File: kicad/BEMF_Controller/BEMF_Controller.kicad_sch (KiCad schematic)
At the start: 110 parts, among them J1 HEADER4VALULOK, J2 HEADER6, J3 FUSE, J4 Coil_A, J5 Coil_B, J6 Coil_C, J7 Vin, Q1 IGBT-TO-247, Q2 IGBT-TO-247, Q3 IGBT-TO-247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

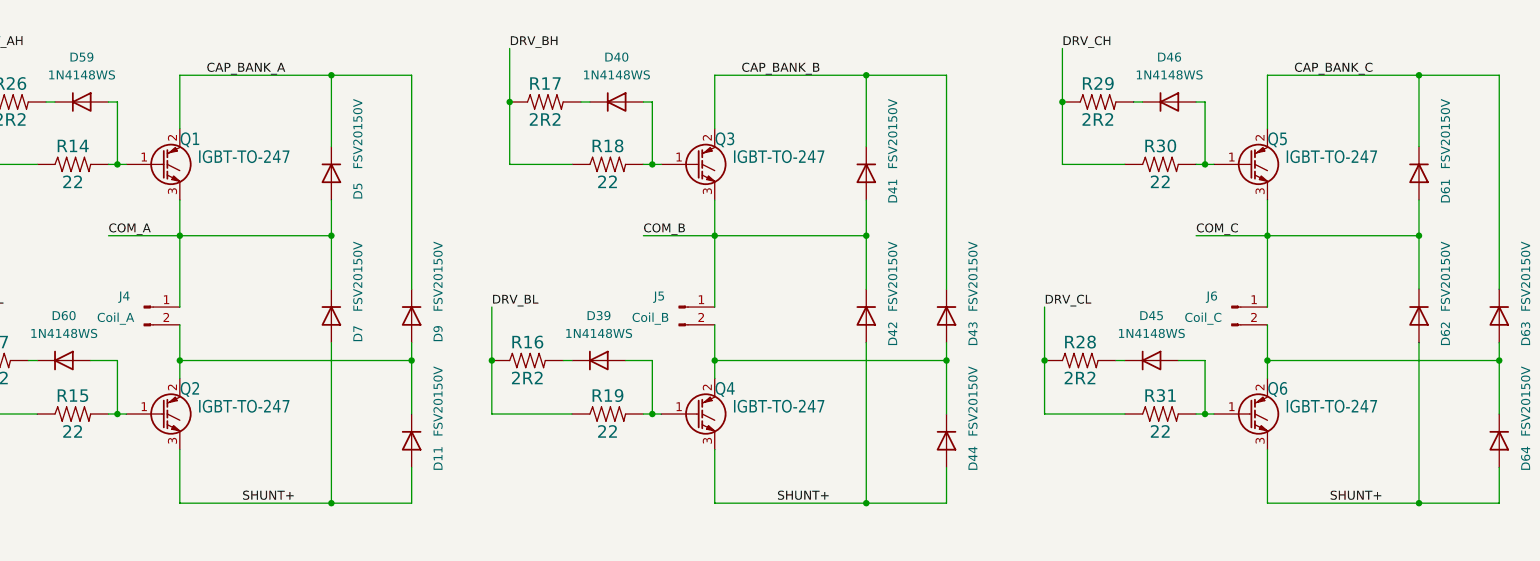
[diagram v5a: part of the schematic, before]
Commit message: Change to mosfets.
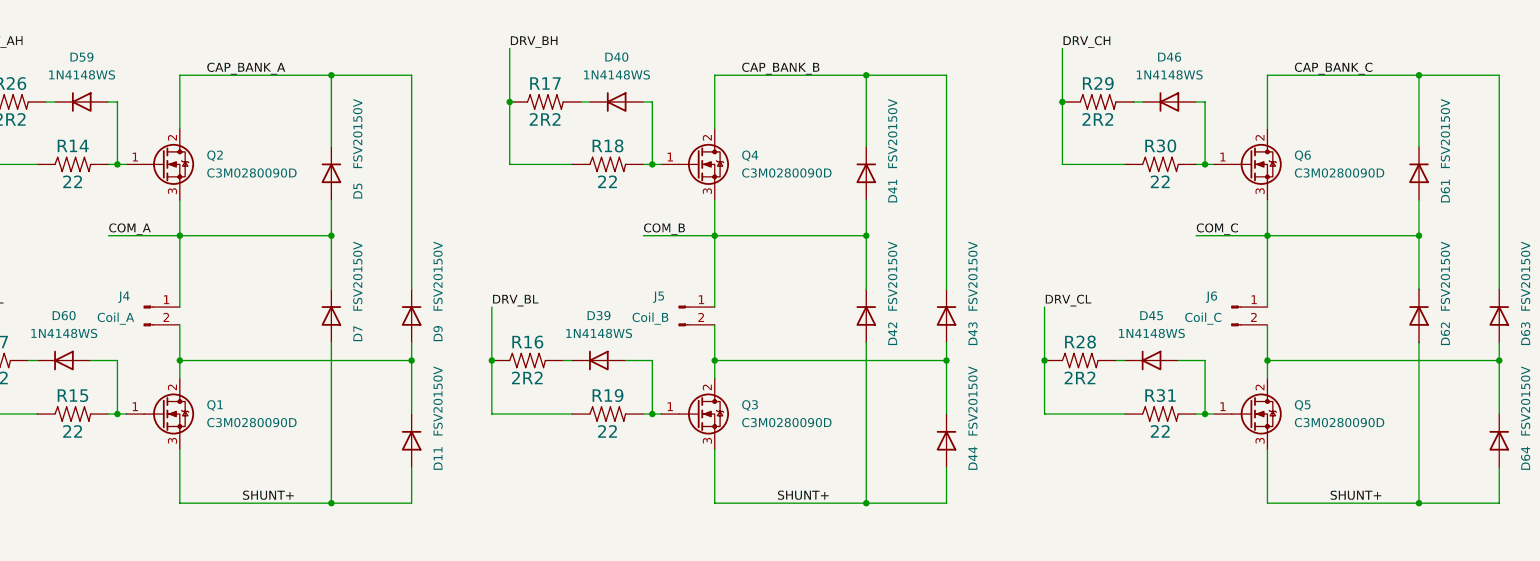
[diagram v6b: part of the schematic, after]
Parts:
- removed Q1, Q2, Q3, Q4, Q5, Q6: IGBT-TO-247, Package_TO_SOT_THT:TO-247-3_Vertical, symbol Transistor_IGBT:IRG4PF50W
- added Q1, Q2, Q3, Q4, Q5, Q6: C3M0280090D, Package_TO_SOT_THT:TO-247-3_Horizontal_TabDown, symbol Transistor_FET:C3M0280090D
- JP7: footprint Connector_PinHeader_2.54mm:PinHeader_1x02_P2.54mm_Vertical -> Jumper:SolderJumper-2_P1.3mm_Open_RoundedPad1.0x1.5mm
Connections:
- net CAP_BANK_A: now also Q2.2 (D)
- net CAP_BANK_B: now also Q4.2 (D)
- net CAP_BANK_C: now also Q6.2 (D)
- net COM_A: now also Q2.3 (S)
- net COM_B: now also Q4.3 (S)
- net COM_C: now also Q6.3 (S)
- net SHUNT+: now also Q1.3 (S), Q3.3 (S), Q5.3 (S)
- net at D40.2 (A), R18.2: now also Q4.1 (G)
- net at D43.2 (A), D44.1 (K), J5.2 (Pin_2): now also Q3.2 (D)
- net at D63.2 (A), D64.1 (K), J6.2 (Pin_2): now also Q5.2 (D)
- net at D11.1 (K), D9.2 (A), J4.2 (Pin_2): now also Q1.2 (D)
- net at D39.2 (A), R19.2: now also Q3.1 (G)
- net at D60.2 (A), R15.2: now also Q1.1 (G)
- net at D46.2 (A), R30.2: now also Q6.1 (G)
- net at D59.2 (A), R14.2: now also Q2.1 (G)
- net at D45.2 (A), R31.2: now also Q5.1 (G)

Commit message: Updated Shottky footprint
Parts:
- removed D39, D40, D45, D46, D59, D60: 1N4148WS, Diode_SMD:D_SOD-323F, symbol Device:D
- removed D41, D42, D43, D44, D61, D62, D63, D64: FSV20150V, Package_TO_SOT_SMD:TO-277A, symbol Device:D
- removed R14, R18, R19, R30, R31: 22, main:1206, symbol main-eagle-import:RESISTOR1206
- removed R16, R17, R26, R27, R28, R29: 2R2, main:1206, symbol main-eagle-import:RESISTOR1206
- added D39, D40, D41, D42, D43, D44, D45, D46: FSV20150V, Package_TO_SOT_SMD:TO-277A, symbol Component_Library:FSV20150V
- added R14, R16, R17, R18, R19: 10, Resistor_THT:R_Axial_DIN0411_L9.9mm_D3.6mm_P15.24mm_Horizontal, symbol Component_Library:ROX1SJ10R
- C1, C11, C12, C14, C15, C16, C17, C18, C19, C2, C20, C3: footprint main:1206 -> Capacitor_SMD:C_1812_4532Metric; symbol main-eagle-import:1.0UF-1206-50V-10% -> Component_Library:CHV1812N250105MXT
- C9: footprint main:1206 -> Capacitor_SMD:C_0805_2012Metric; symbol main-eagle-import:1.0UF-1206-50V-10% -> Component_Library:CHV1812N250105MXT
- D11, D5, D7, D9: symbol Device:D -> Component_Library:FSV20150V
- R15: value 22 -> 10; footprint main:1206 -> Resistor_THT:R_Axial_DIN0411_L9.9mm_D3.6mm_P15.24mm_Horizontal; symbol main-eagle-import:RESISTOR1206 -> Component_Library:ROX1SJ10R
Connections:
- net CAP_BANK_A: now also D5.2 (A), D9.2 (A)
- net CAP_BANK_B: now also Q3.2 (D), D39.1 (A), D39.2 (A), D41.1 (A), D41.2 (A); no longer Q4.2 (D)
- net CAP_BANK_C: now also Q5.2 (D), D43.1 (A), D43.2 (A), D45.1 (A), D45.2 (A); no longer Q6.2 (D)
- net COM_A: now also D5.3 (K), D7.2 (A); no longer D5.2 (A)
- net COM_B: now also Q3.3 (S), D39.3 (K), D40.1 (A), D40.2 (A); no longer Q4.3 (S)
- net COM_C: now also Q5.3 (S), D43.3 (K), D44.1 (A), D44.2 (A); no longer Q6.3 (S)
- net DRV_AH: now also R14.2
- net DRV_AL: now also R15.2; no longer R15.1
- net DRV_BH: now also R16.2
- net DRV_BL: now also R17.2
- net DRV_CH: now also R18.2
- net DRV_CL: now also R19.2
- net SHUNT+: now also D11.3 (K), D7.3 (K), Q4.3 (S), Q6.3 (S), D40.3 (K), D42.3 (K), D44.3 (K), D46.3 (K); no longer D11.2 (A), D7.2 (A), Q3.3 (S), Q5.3 (S)
- net at J5.2 (Pin_2): now also Q4.2 (D), D41.3 (K), D42.1 (A), D42.2 (A); no longer Q3.2 (D)
- net at J6.2 (Pin_2): now also Q6.2 (D), D45.3 (K), D46.1 (A), D46.2 (A); no longer Q5.2 (D)
- net at Q1.1 (G): now also R15.1; no longer R15.2
- net at D11.1 (A), J4.2 (Pin_2), Q1.2 (D): now also D11.2 (A), D9.3 (K); no longer D9.2 (A)
- net at Q3.1 (G): now also R16.1
- net at Q4.1 (G): now also R17.1
- net at Q2.1 (G): now also R14.1
- net at Q5.1 (G): now also R18.1
- net at Q6.1 (G): now also R19.1

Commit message: Added component library
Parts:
- D49, D50, D53, D54, D57, D58: footprint Diode_SMD:D_SOD-323F -> Diode_SMD:D_SOD-323; symbol Device:D -> Diode:1N4148WS
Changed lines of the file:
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@@
 	)
 	(symbol
-		(lib_id "Device:D")
+		(lib_id "Diode:1N4148WS")
 		(at 372.11 57.15 270)
 		(unit 1)
@@
 			)
 		)
-		(property "Footprint" "Diode_SMD:D_SOD-323F"
-			(at 372.11 57.15 0)
+		(property "Footprint" "Diode_SMD:D_SOD-323"
+			(at 367.665 57.15 0)
 			(effects
 				(font
@@
 			)
 		)
-		(property "Datasheet" "~"
+		(property "Datasheet" "https://www.vishay.com/docs/85751/1n4148ws.pdf"
 			(at 372.11 57.15 0)
 			(effects
@@
 			)
 		)
-		(property "Description" "Diode"
+		(property "Description" "75V 0.15A Fast switching Diode, SOD-323"
 			(at 372.11 57.15 0)
 			(effects
@@
 	)
 	(symbol
-		(lib_id "Device:D")
+		(lib_id "Diode:1N4148WS")
 		(at 372.11 45.72 270)
 		(unit 1)
@@
 			)
 		)
-		(property "Footprint" "Diode_SMD:D_SOD-323F"
-			(at 372.11 45.72 0)
+		(property "Footprint" "Diode_SMD:D_SOD-323"
+			(at 367.665 45.72 0)
 			(effects
 				(font
@@
 			)
 		)
-		(property "Datasheet" "~"
+		(property "Datasheet" "https://www.vishay.com/docs/85751/1n4148ws.pdf"
 			(at 372.11 45.72 0)
 			(effects
@@
 			)
 		)
-		(property "Description" "Diode"
+		(property "Description" "75V 0.15A Fast switching Diode, SOD-323"
 			(at 372.11 45.72 0)
 			(effects
@@
 	)
 	(symbol
-		(lib_id "Device:D")
+		(lib_id "Diode:1N4148WS")
 		(at 325.12 57.15 270)
 		(unit 1)
@@
 			)
 		)
-		(property "Footprint" "Diode_SMD:D_SOD-323F"
-			(at 325.12 57.15 0)
+		(property "Footprint" "Diode_SMD:D_SOD-323"
+			(at 320.675 57.15 0)
 			(effects
 				(font
@@
 			)
 		)
-		(property "Datasheet" "~"
+		(property "Datasheet" "https://www.vishay.com/docs/85751/1n4148ws.pdf"
 			(at 325.12 57.15 0)
 			(effects
@@
 			)
 		)
-		(property "Description" "Diode"
+		(property "Description" "75V 0.15A Fast switching Diode, SOD-323"
 			(at 325.12 57.15 0)
 			(effects
@@
 	)
 	(symbol
-		(lib_id "Device:D")
+		(lib_id "Diode:1N4148WS")
 		(at 325.12 45.72 270)
 		(unit 1)
@@
 			)
 		)
-		(property "Footprint" "Diode_SMD:D_SOD-323F"
-			(at 325.12 45.72 0)
+		(property "Footprint" "Diode_SMD:D_SOD-323"
+			(at 320.675 45.72 0)
 			(effects
 				(font
@@
 			)
 		)
-		(property "Datasheet" "~"
+		(property "Datasheet" "https://www.vishay.com/docs/85751/1n4148ws.pdf"
 			(at 325.12 45.72 0)
 			(effects
@@
 			)
 		)
-		(property "Description" "Diode"
+		(property "Description" "75V 0.15A Fast switching Diode, SOD-323"
 			(at 325.12 45.72 0)
 			(effects
@@
 	)
 	(symbol
-		(lib_id "Device:D")
+		(lib_id "Diode:1N4148WS")
 		(at 275.59 45.72 270)
 		(unit 1)
@@
 			)
 		)
-		(property "Footprint" "Diode_SMD:D_SOD-323F"
-			(at 275.59 45.72 0)
+		(property "Footprint" "Diode_SMD:D_SOD-323"
+			(at 271.145 45.72 0)
 			(effects
 				(font
@@
 			)
 		)
-		(property "Datasheet" "~"
+		(property "Datasheet" "https://www.vishay.com/docs/85751/1n4148ws.pdf"
 			(at 275.59 45.72 0)
 			(effects
@@
 			)
 		)
-		(property "Description" "Diode"
+		(property "Description" "75V 0.15A Fast switching Diode, SOD-323"
 			(at 275.59 45.72 0)
 			(effects
@@
 	)
 	(symbol
-		(lib_id "Device:D")
+		(lib_id "Diode:1N4148WS")
 		(at 275.59 57.15 270)
 		(unit 1)
@@
 			)
 		)
-		(property "Footprint" "Diode_SMD:D_SOD-323F"
-			(at 275.59 57.15 0)
+		(property "Footprint" "Diode_SMD:D_SOD-323"
+			(at 271.145 57.15 0)
 			(effects
 				(font
@@
 			)
 		)
-		(property "Datasheet" "~"
+		(property "Datasheet" "https://www.vishay.com/docs/85751/1n4148ws.pdf"
 			(at 275.59 57.15 0)
 			(effects
@@
 			)
 		)
-		(property "Description" "Diode"
+		(property "Description" "75V 0.15A Fast switching Diode, SOD-323"
 			(at 275.59 57.15 0)
 			(effects
